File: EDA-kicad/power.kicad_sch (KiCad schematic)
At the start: 84 parts, among them SW6 CHP-041B, U10 BAT-CONNECTOR-FLTS22WR00, U11 BQ25792RQMR, U2 TPS650250RHBR

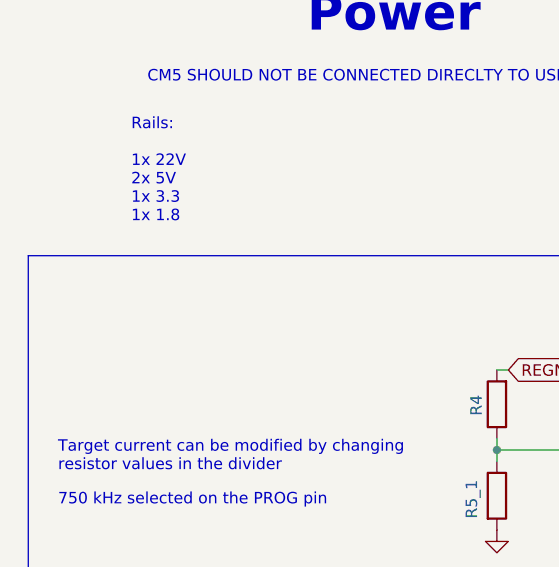
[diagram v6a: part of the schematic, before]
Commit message: add charger IC label
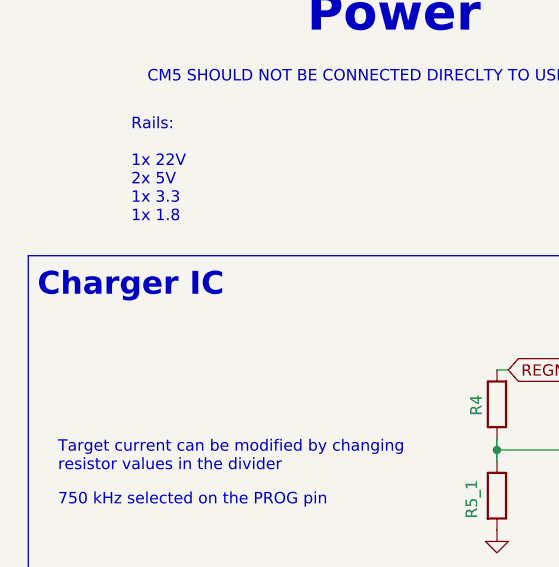
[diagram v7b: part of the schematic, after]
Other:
- note added: "Charger IC"
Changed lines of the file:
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@@
 		)
 	)
+	(text "Charger IC"
+		(exclude_from_sim no)
+		(at 18.796 54.102 0)
+		(effects
+			(font
+				(face "KiCad Font")
+				(size 2.54 2.54)
+				(thickness 0.508)
+				(bold yes)
+			)
+			(justify left)
+		)
+	)
 	(text "PSM mode selected"
 		(exclude_from_sim no)
@@
 		(effects
 			(font
+				(face "KiCad Font")
 				(size 2.54 2.54)
 				(thickness 0.508)
@@
 			"AAAAtI4EBwAAAAAAQOtIcAAAAAAAALSOBAcAAAAAAEDrSHAAAAAAAAC0jgQHAAAAAABA60hwAAAA"
 			"AAAAtE5v7AIAANA0VVUVRTEYDIqiqKpq7HIA5FeSJMmyrNPpZFmWJMnY5QAA8p//AwsWj5K+1Aeb"
-			"AAAAAElFTkSuQmCC"
+			"AAAAAElFTkSuQmCCAAAyAAAANwAAAGQAAAArAAAASQAAAGUAAABNAAAAUgAAAFIAAABGAAAAcQAA"
+			"AGEAAABtAAAAcAAAAEYAAABXAAAAOQAAAC8AAAAvAAAALwAAADcAAAA5AAAAcwAAAFcAAABQAAAA"
+			"SAAAADUAAABPAAAAVAAAAGsAAABYAAAAcgAAADkAAAArAAAALwAAAGMAAAA4AAAALwAAAC8AAAB4"
+			"AAAAUQAAAFYAAABGAAAAUgAAADAAAAA5AAAAZQAAAGwAAABSAAAAUgAAAFUAAABiAAAASAAAAG0A"
+			"AABlAAAAMgAAAFkAAABZAAAAWgAAAHMAAABPAAAARwAAAEQAAABaAAAAcwAAADIAAABiAAAAVwAA"
+			"AHIAAABmAAAAdgAAAHIAAAAyAAAAegAAAHMAAAA3AAAATwAAAGoAAABvAAAANgAAAE8AAABtAAAA"
+			"cAAAAGkAAABZAAAAaAAAAFIAAABGAAAATgAAAFQAAABjAAAAKwAAAHoAAABZAAAAcwAAAFcAAABQ"
+			"AAAASAAAAGoAAABrAAAAMQAAAEoAAABTAAAAYgAAAGwAAAB3AAAANAAAAFUAAABKAAAAZwAAAFkA"
+			"AABPAAAARAAAAGQAAAB1AAAAMwAAAGMAAAB4AAAALwAAADQAAAB0AAAAWQAAAGMAAABlAAAAOAAA"
+			"AGsAAABKAAAARAAAAGcAAABnAAAASwAAAFMAAABRAAAANAAAAEEAAABEAAAAOAAAAGIAAABKAAAA"
+			"aQAAADEAAABpAAAAMwAAAFUAAABpAAAAbgAAAGUAAAAyAAAANwAAAHoAAABaAAAAbwAAADkAAAAz"
+			"AAAANgAAAEQAAABSAAAAawAAAFcAAABwAAAAZQAAAGgAAAA0AAAAcwAAADAAAABpAAAAUQAAAGMA"
+			"AAA2AAAAYgAAADYAAAAzAAAAdAAAADgAAAB2AAAATAAAAGIAAAA0AAAAUAAAAHMAAABpAAAAcwAA"
+			"AFQAAABYAAAAegAAAEMAAABhAAAAVwAAAFgAAABYAAAAUwAAAGEAAAB2AAAAZwAAAGIAAABuAAAA"
+			"aAAAAGsAAABOAAAAVQAAADkAAABoAAAAaAAAAEsAAAA4AAAATwAAAFQAAAB4AAAAcgAAAE8AAAAr"
+			"AAAAOAAAAE4AAAByAAAANAAAAFYAAABDAAAAYgAAAFkAAABiAAAAUAAAAGEAAABEAAAAUwAAAE8A"
+			"AABFAAAARQAAAEIAAABFAAAALwAAAE4AAABmAAAAYgAAADQAAABtAAAAdgAAAG4AAABMAAAAVAAA"
+			"ADcAAAAzAAAANgAAAGkAAAByAAAAZgAAAHcAAABQAAAAQgAAADUAAAB2AAAAdwAAAG8AAABRAAAA"
+			"SgAAAFYAAABsAA=="
 		)
 	)

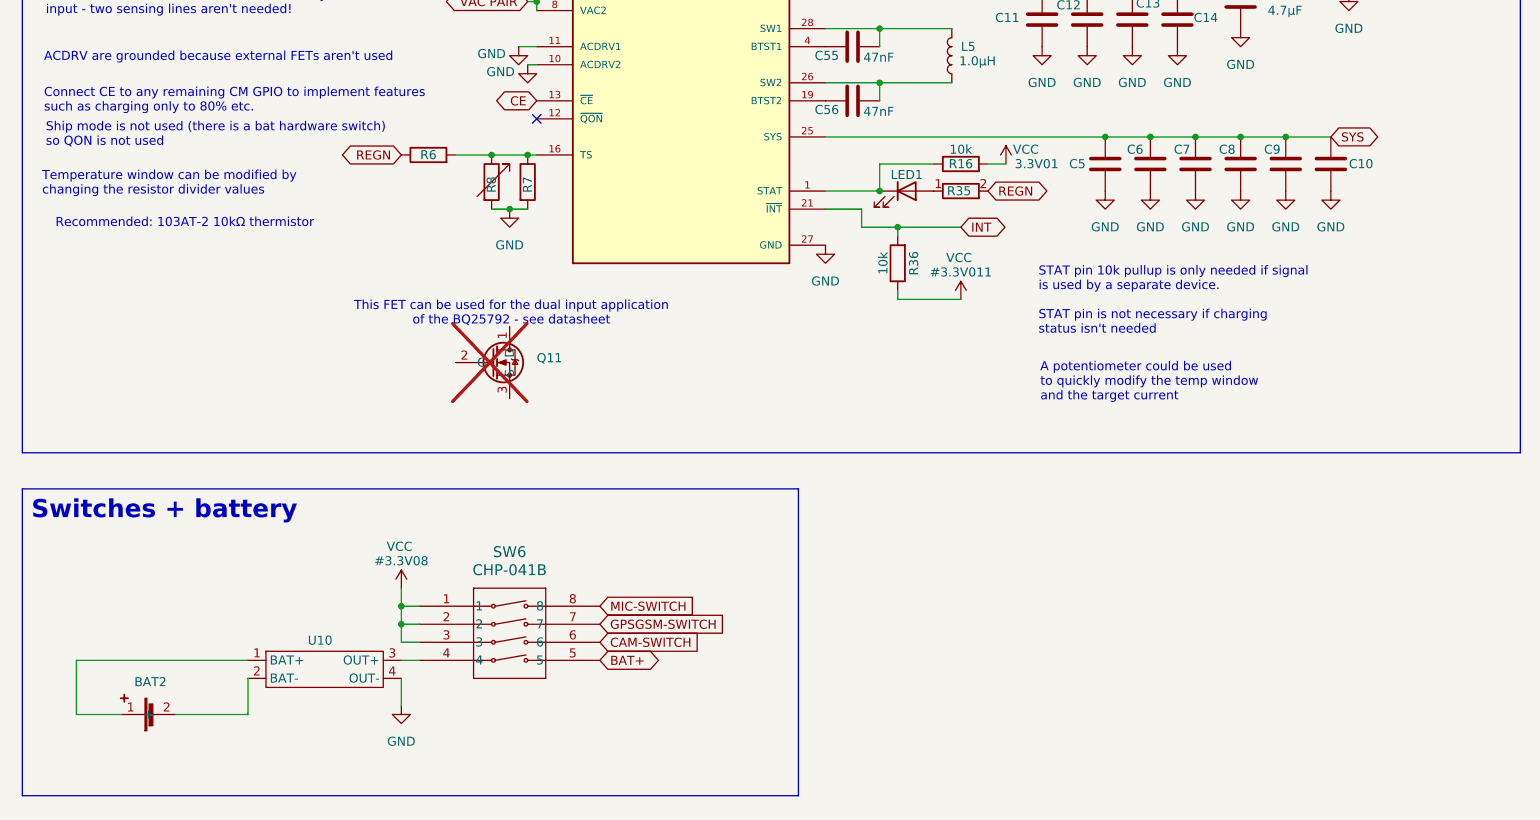
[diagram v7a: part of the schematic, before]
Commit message: add fields to some symbols
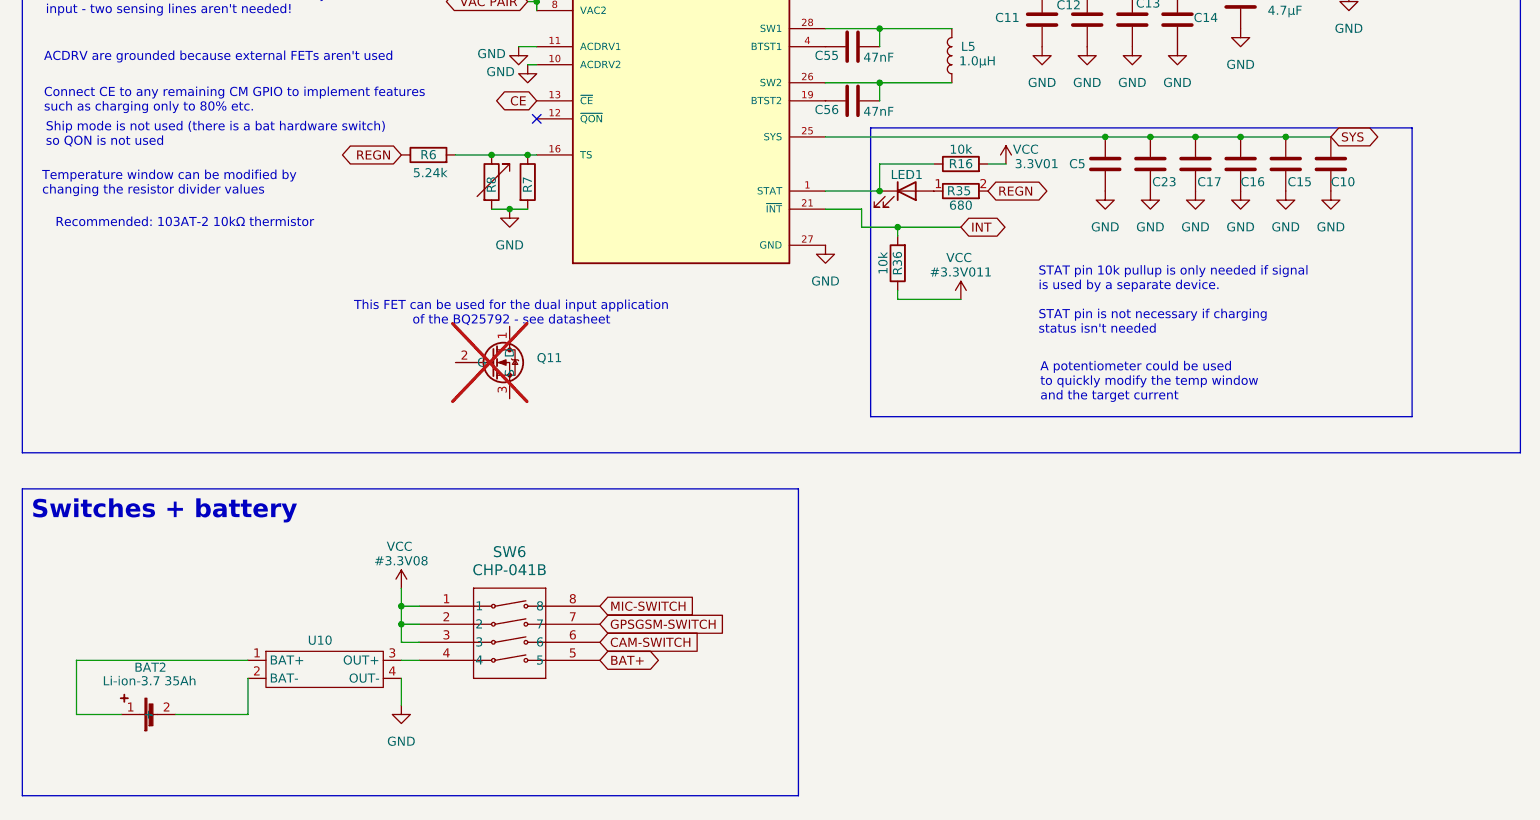
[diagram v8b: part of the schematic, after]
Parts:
- removed C6, C7, C8, C9: 10μF, SPIRIT-footprints:USBC_capacitor_CAPC0603X33N, symbol Device:C
- added C15, C16, C17, C23: 10μF, SPIRIT-footprints:USBC_capacitor_CAPC0603X33N, symbol Device:C
- BAT2: value battery_37V3500mAhLP685077JU -> Li-ion-3.7 35Ah; MPN (none) -> LP504783JU
- C10: MPN (none) -> CC0603KRX5R6BB106
- C5: MPN (none) -> CC0603KRX7R7BB104
- LED1: value LED -> 5mA 2V Fv; MPN (none) -> QBLP601-R5
- R16, R36: footprint (none) -> SPIRIT-footprints:0603-resistor; MPN (none) -> ERA-3AEB103V
- R35: value 0603-resistor-680ohm-ERJ3EKF6800V -> 680; MPN (none) -> ERJ3EKF6800V
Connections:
- net AGND: now also C15.2, C16.2, C17.2, C23.2
- net SYS: now also C15.1, C16.1, C17.1, C23.1
